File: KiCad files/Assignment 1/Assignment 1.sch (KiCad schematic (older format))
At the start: 20 parts, among them SW1 SW_Push, SW2 SW_Push, U1 CC56-12EWA

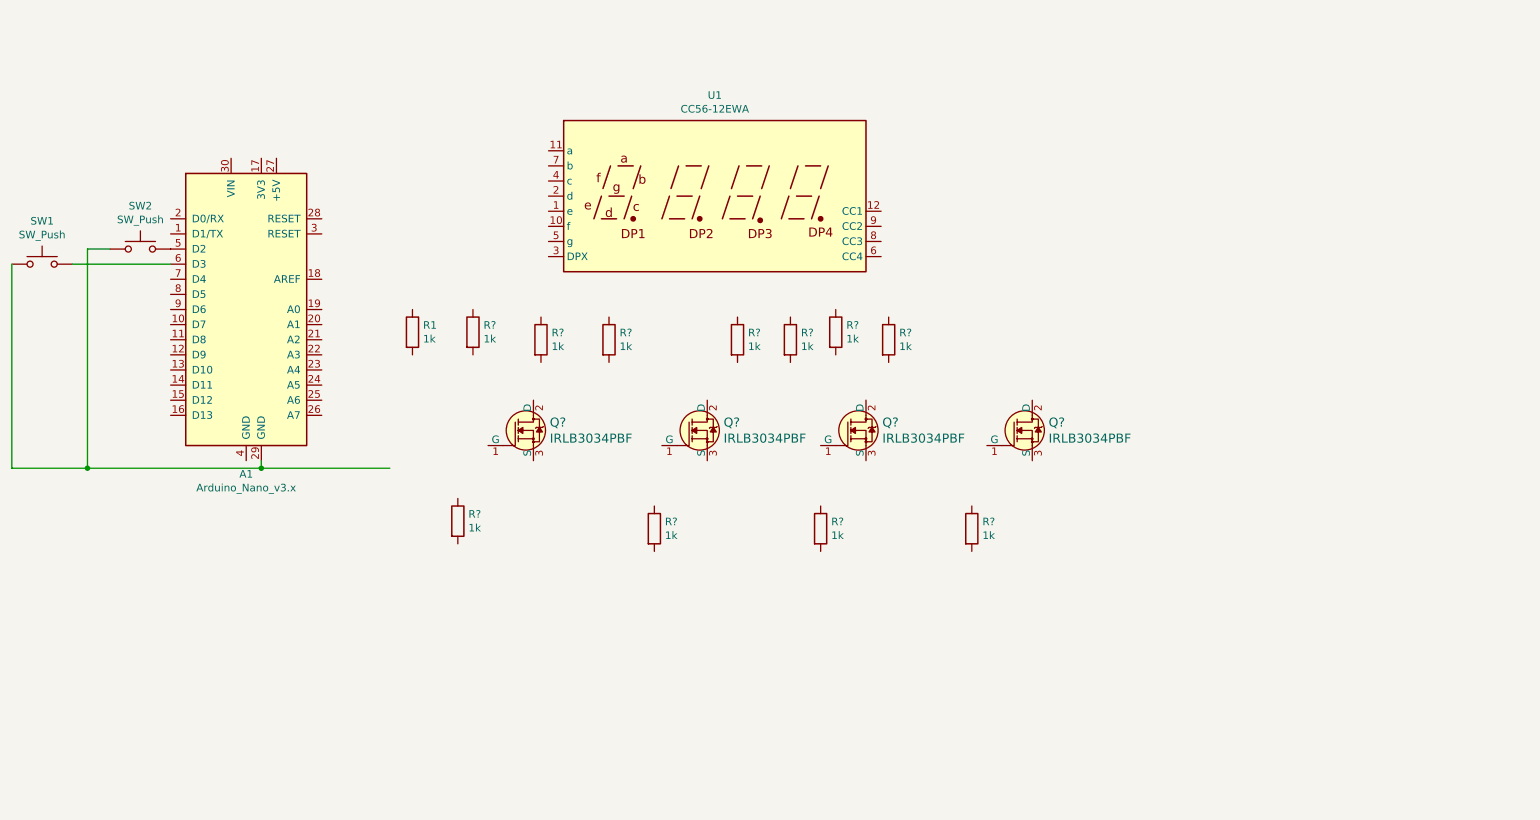
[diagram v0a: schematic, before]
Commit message: Fixed KiCad project file clash issue Added code to ReadMe
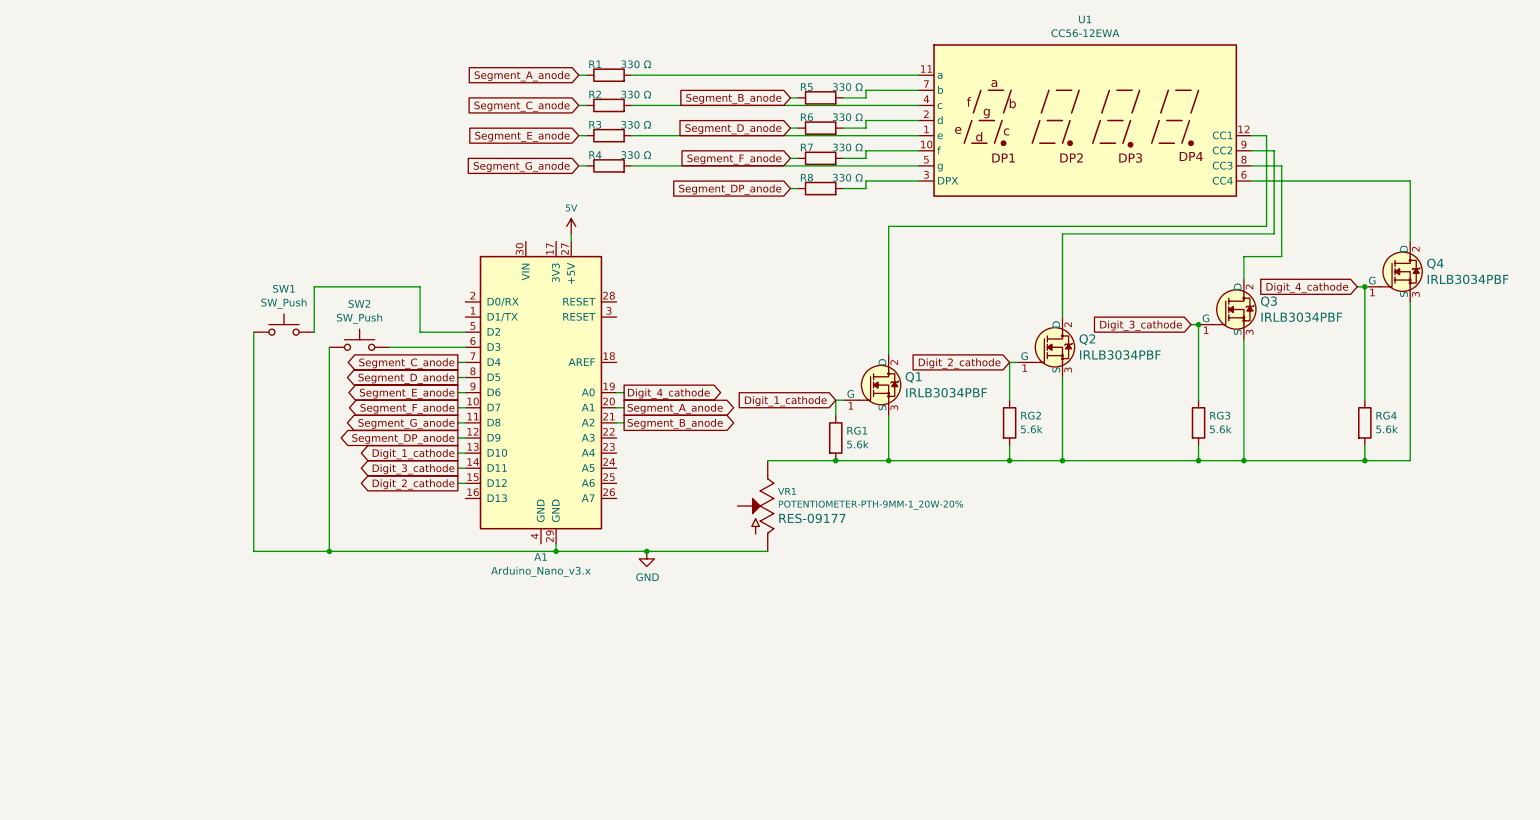
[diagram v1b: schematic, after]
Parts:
- removed R1, R? (x9): 1k, Resistor_THT:R_Axial_DIN0204_L3.6mm_D1.6mm_P5.08mm_Horizontal, symbol Device:R
- added R2, R3, R4, R5, R6, R7, R8: 330 Ω, Resistor_THT:R_Axial_DIN0204_L3.6mm_D1.6mm_P5.08mm_Horizontal, symbol Device:R
- added RG2, RG3, RG4: 5.6k, Resistor_THT:R_Axial_DIN0204_L3.6mm_D1.6mm_P5.08mm_Horizontal, symbol Device:R
- added VR1: POTENTIOMETER-PTH-9MM-1_20W-20%, Potentiometer_THT:Potentiometer_Bourns_3339H_Vertical, symbol SparkFun-Resistors:POTENTIOMETER-PTH-9MM-1_20W-20%
- R1: renamed from R?; value 1k -> 330 Ω
- RG1: renamed from R?; value 1k -> 5.6k
- gave numbers to parts that had none: 4
- renumbered SW2 to SW1, SW1 to SW2
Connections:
- net labels added: 5V, Digit_1_cathode, Digit_2_cathode, Digit_3_cathode, Digit_4_cathode, GND, Segment_A_anode, Segment_B_anode, Segment_C_anode, Segment_DP_anode, Segment_D_anode, Segment_E_anode, Segment_F_anode, Segment_G_anode
- wire segments 8 -> 86
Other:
- moved on the sheet: A1, Q1, Q2, Q3, Q4, R1, RG1, SW1, SW2, U1

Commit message: Added images of the schematic and the 3D view
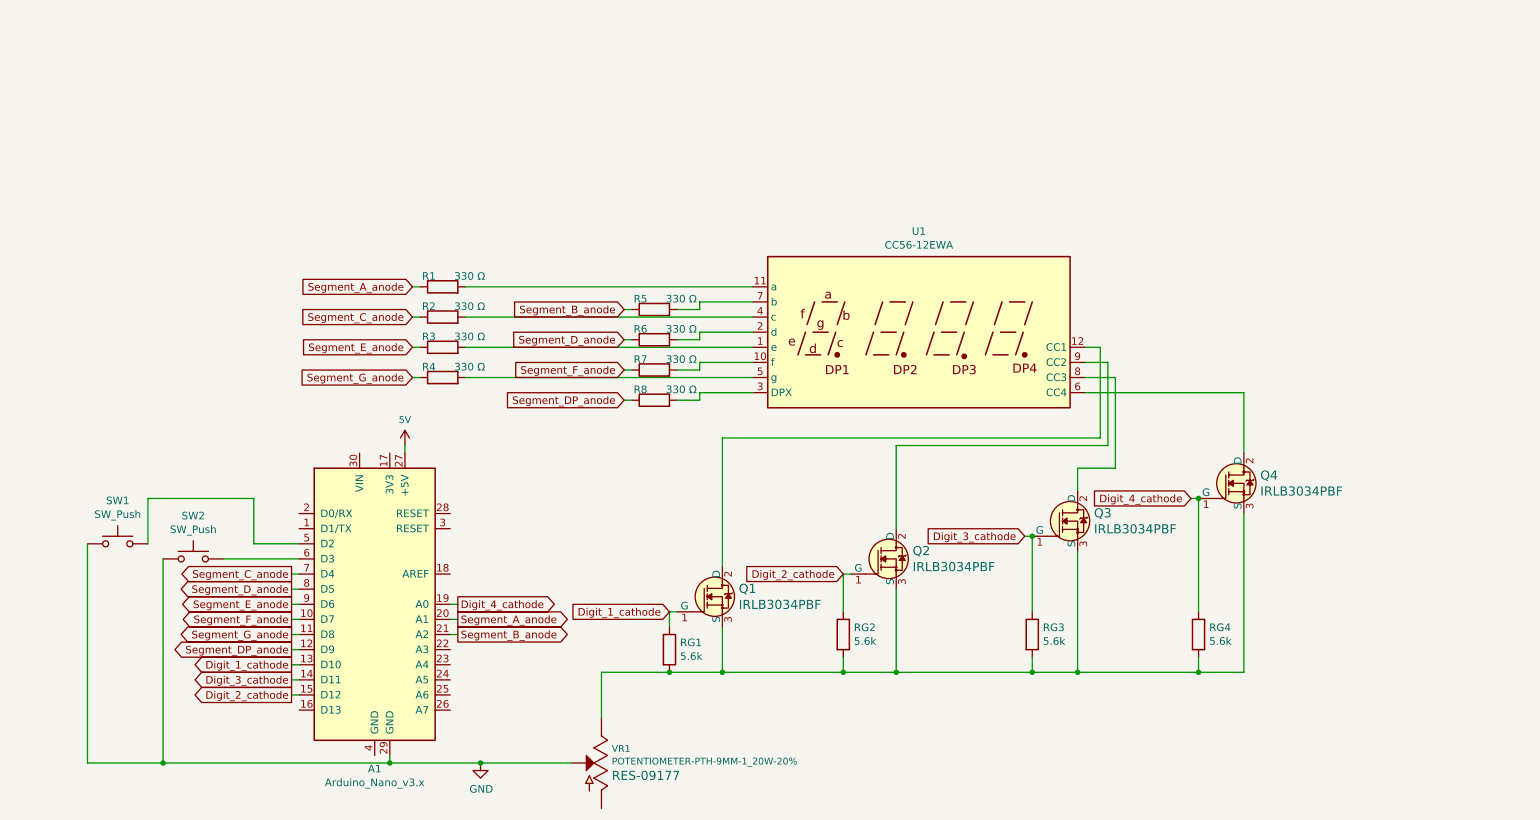
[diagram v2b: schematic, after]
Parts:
- Q1, Q2, Q3, Q4: footprint Silicon-Standard:SOT23-3 -> Silicon-Standard:TO-220-ALT
- VR1: footprint Potentiometer_THT:Potentiometer_Bourns_3339H_Vertical -> Potentiometer_THT:Potentiometer_Bourns_3339P_Vertical_HandSoldering
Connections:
- net GND: now also VR1.P$2 (S); no longer VR1.P$3 (A)
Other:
- moved on the sheet: A1, Q1, Q2, Q3, Q4, R1, R2, R3, R4, R5, R6, R7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
